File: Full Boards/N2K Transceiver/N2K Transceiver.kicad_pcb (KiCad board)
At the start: 4 copper layers, 80 x 60 mm, 73 parts, among them J1 JTAG, SW1 SW_MEC_5G, SW2 SW_MEC_5G, SW3 SW_MEC_5G

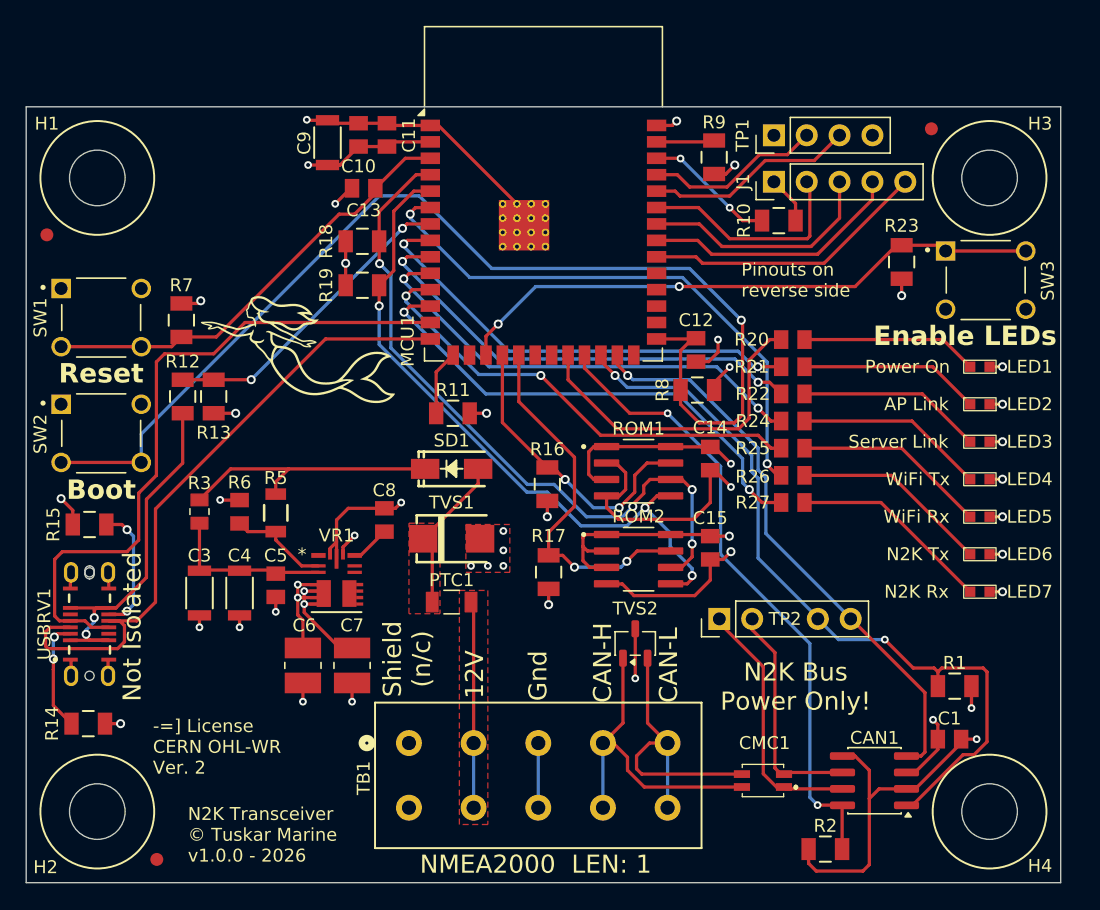
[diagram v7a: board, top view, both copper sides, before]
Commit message: Updated annotations after the RC removal.
Signed-off-by: digimer <digital.mermaid@gmail.com>
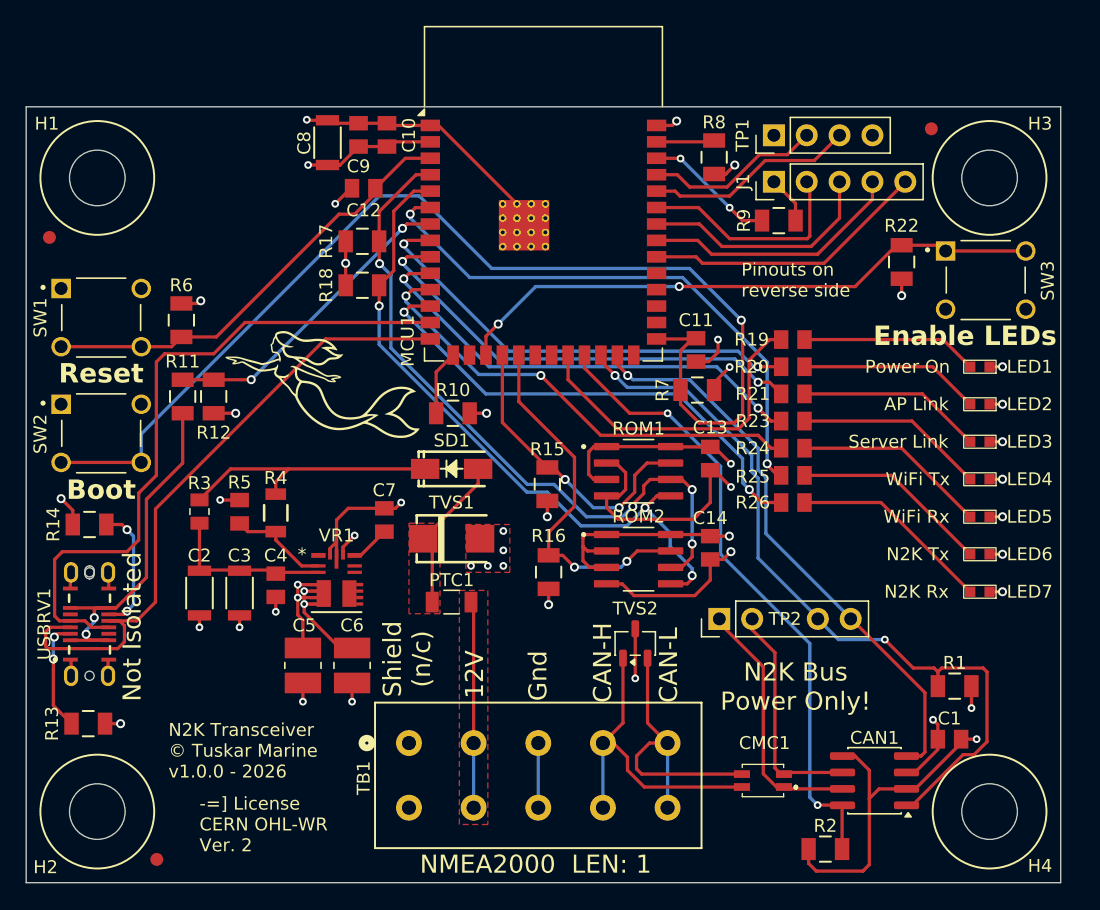
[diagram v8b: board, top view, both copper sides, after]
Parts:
- moved REF** 3.30 mm to (64.4, 53.3)
- moved FID2 0.28 mm to (61.8, 53.4)
- renumbered C11 to C10, C12 to C11, C13 to C12, C14 to C13, C15 to C14, C3 to C2, C4 to C3, C5 to C4, C6 to C5, C7 to C6, C8 to C7, C9 to C8, C10 to C9, R11 to R10, R12 to R11, R13 to R12, R14 to R13, R15 to R14, R16 to R15, R17 to R16, R18 to R17, R19 to R18, R20 to R19, R21 to R20, R22 to R21, R23 to R22, R24 to R23, R25 to R24, R26 to R25, R27 to R26, R5 to R4, R6 to R5, R7 to R6, R8 to R7, R9 to R8, R10 to R9
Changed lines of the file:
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@@
 		(layer "F.Cu")
 		(at 119.3 69.7)
-		(property "Reference" "R25"
+		(property "Reference" "R24"
 			(at -3.1162 0 0)
 			(unlocked yes)
@@
 		(at 100.3 72.480916 90)
 		(tags "RNCP1206FTD3K01 ")
-		(property "Reference" "R16"
+		(property "Reference" "R15"
 			(at 2.7 0 0)
 			(unlocked yes)
@@
 		(at 127.7 55.3 -90)
 		(tags "RNCP1206FTD3K01 ")
-		(property "Reference" "R23"
+		(property "Reference" "R22"
 			(at -2.8 0 0)
 			(unlocked yes)
@@
 		(layer "F.Cu")
 		(at 79.3 74.7 90)
-		(property "Reference" "R5"
+		(property "Reference" "R4"
 			(at 2.7 0 180)
 			(layer "F.SilkS")
@@
 		(at 112.9 70.5 90)
 		(tags "08051C105K4Z2A ")
-		(property "Reference" "C14"
+		(property "Reference" "C13"
 			(at 2.4 0 0)
 			(unlocked yes)
@@
 		(at 87.7 75.25 90)
 		(tags "08051C105K4Z2A ")
-		(property "Reference" "C8"
+		(property "Reference" "C7"
 			(at 2.3 0 0)
 			(unlocked yes)
@@
 		(at 111.8 62.1 -90)
 		(tags "08051C105K4Z2A ")
-		(property "Reference" "C12"
+		(property "Reference" "C11"
 			(at -2.3 0 0)
 			(unlocked yes)
@@
 		(layer "F.Cu")
 		(at 119.3 71.8)
-		(property "Reference" "R26"
+		(property "Reference" "R25"
 			(at -3.1162 0.1 0)
 			(unlocked yes)
@@
 	(footprint "Fiducial:Fiducial_1mm_Mask2mm"
 		(layer "F.Cu")
-		(at 61.6 53.2)
+		(at 61.8 53.4)
 		(descr "Fiducial, circular marking, 1mm bare copper, 2mm soldermask opening (Level A)")
 		(tags "fiducial")
@@
 		(at 64.8 91)
 		(tags "RNCP1206FTD3K01 ")
-		(property "Reference" "R14"
+		(property "Reference" "R13"
 			(at -2.8 0 90)
 			(unlocked yes)
@@
 		(at 85.7 45.472 90)
 		(tags "08051C105K4Z2A ")
-		(property "Reference" "C10"
+		(property "Reference" "C9"
 			(at -2.428 0 0)
 			(unlocked yes)
@@
 		(layer "F.Cu")
 		(at 119.3 63.4)
-		(property "Reference" "R21"
+		(property "Reference" "R20"
 			(at -3.2 0 0)
 			(unlocked yes)
@@
 		(at 118.2 52.1 180)
 		(tags "RNCP1206FTD3K01 ")
-		(property "Reference" "R10"
+		(property "Reference" "R9"
 			(at 2.7 0 90)
 			(unlocked yes)
@@
 		(at 86.1 49.6 180)
 		(tags "08051C105K4Z2A ")
-		(property "Reference" "C13"
+		(property "Reference" "C12"
 			(at 0 -1.7 0)
 			(unlocked yes)
@@
 		(at 113.2 47.2 90)
 		(tags "RNCP1206FTD3K01 ")
-		(property "Reference" "R9"
+		(property "Reference" "R8"
 			(at 2.7 0 0)
 			(unlocked yes)
@@
 		(at 112.9 77.4 90)
 		(tags "08051C105K4Z2A ")
-		(property "Reference" "C15"
+		(property "Reference" "C14"
 			(at 2.3 0 0)
 			(unlocked yes)
@@
 		(layer "F.Cu")
 		(at 119.3 65.5)
-		(property "Reference" "R22"
+		(property "Reference" "R21"
 			(at -3.1162 0 0)
 			(unlocked yes)
@@
 		(at 73.4 80.9 -90)
 		(tags "CGA5L1X7R1H106K160AE ")
-		(property "Reference" "C3"
+		(property "Reference" "C2"
 			(at -2.9 0 0)
 			(unlocked yes)
@@
 		(at 83.3 46.072 -90)
 		(tags "CGA5L1X7R1H106K160AE ")
-		(property "Reference" "C9"
+		(property "Reference" "C8"
 			(at 0.028 1.8 90)
 			(unlocked yes)
@@
 		(at 111.9 65.2)
 		(tags "RNCP1206FTD3K01 ")
-		(property "Reference" "R8"
+		(property "Reference" "R7"
 			(at -2.7 0 90)
 			(unlocked yes)
@@
 		(at 93 67 180)
 		(tags "RNCP1206FTD3K01 ")
-		(property "Reference" "R11"
+		(property "Reference" "R10"
 			(at 0 1.8 0)
 			(unlocked yes)
@@
 	(footprint "mr-stuff:Mermaid Silkscreen - 10mm"
 		(layer "F.Cu")
-		(at 62.52748 50.638629)
+		(at 64.42748 53.338629)
 		(property "Reference" "REF**"
 			(at 0 -0.5 0)
@@
 		(at 76.5 80.9 -90)
 		(tags "CGA5L1X7R1H106K160AE ")
-		(property "Reference" "C4"
+		(property "Reference" "C3"
 			(at -2.9 0 0)
 			(unlocked yes)
@@
 		(at 86 53.7 180)
 		(tags "RNCP1206FTD3K01 ")
-		(property "Reference" "R18"
+		(property "Reference" "R17"
 			(at 2.8 0 90)
 			(unlocked yes)
@@
 		(layer "F.Cu")
 		(at 119.3 67.6)
-		(property "Reference" "R24"
+		(property "Reference" "R23"
 			(at -3.1 0 0)
 			(unlocked yes)
@@
 		(layer "F.Cu")
 		(at 76.5 74.6 90)
-		(property "Reference" "R6"
+		(property "Reference" "R5"
 			(at 2.2537 0 0)
 			(unlocked yes)
@@
 		(at 72.1 65.7 90)
 		(tags "RNCP1206FTD3K01 ")
-		(property "Reference" "R12"
+		(property "Reference" "R11"
 			(at 2.7 0 0)
 			(unlocked yes)
@@
 		(layer "F.Cu")
 		(at 119.3 73.9)
-		(property "Reference" "R27"
+		(property "Reference" "R26"
 			(at -3.1162 0 0)
 			(unlocked yes)
@@
 		(layer "F.Cu")
 		(at 85.2 86.5 -90)
-		(property "Reference" "C7"
+		(property "Reference" "C6"
 			(at -3.1 0 0)
 			(layer "F.SilkS")
@@
 		(layer "F.Cu")
 		(at 81.4 86.5 -90)
-		(property "Reference" "C6"
+		(property "Reference" "C5"
 			(at -3.1 -0.1 0)
 			(layer "F.SilkS")
@@
 		(at 86 57.1 180)
 		(tags "RNCP1206FTD3K01 ")
-		(property "Reference" "R19"
+		(property "Reference" "R18"
 			(at 2.8 0 90)
 			(unlocked yes)
@@
 		(at 100.4 79.280916 90)
 		(tags "RNCP1206FTD3K01 ")
-		(property "Reference" "R17"
+		(property "Reference" "R16"
 			(at 2.8 0 0)
 			(unlocked yes)
@@
 		(at 79.3 80.3 -90)
 		(tags "08051C105K4Z2A ")
-		(property "Reference" "C5"
+		(property "Reference" "C4"
 			(at -2.3 0 0)
 			(unlocked yes)
@@
 		(at 72 59.8 90)
 		(tags "RNCP1206FTD3K01 ")
-		(property "Reference" "R7"
+		(property "Reference" "R6"
 			(at 2.7 0 0)
 			(unlocked yes)
@@
 		(at 64.9 75.6 180)
 		(tags "RNCP1206FTD3K01 ")
-		(property "Reference" "R15"
+		(property "Reference" "R14"
 			(at 2.8 0 90)
 			(unlocked yes)
@@
 		(layer "F.Cu")
 		(at 119.3 61.3)
-		(property "Reference" "R20"
+		(property "Reference" "R19"
 			(at -3.2 0 0)
 			(unlocked yes)
@@
 		(at 74.5 65.7 90)
 		(tags "RNCP1206FTD3K01 ")
-		(property "Reference" "R13"
+		(property "Reference" "R12"
 			(at -2.8 0 0)
 			(unlocked yes)
@@
 		(at 87.9 45.472 90)
 		(tags "08051C105K4Z2A ")
-		(property "Reference" "C11"
+		(property "Reference" "C10"
 			(at -0.028 1.7 90)
 			(unlocked yes)
@@
 		(layer "Edge.Cuts")
 	)
-	(gr_text "-=] License\nCERN OHL-WR\nVer. 2\n"
-		(at 69.8 90.6 0)
+	(gr_text "N2K Transceiver\n© Tuskar Marine\nv1.0.0 - 2026"
+		(at 71 90.9 0)
 		(layer "F.SilkS")
 		(effects
@@
 		)
 	)
-	(gr_text "N2K Transceiver\n© Tuskar Marine\nv1.0.0 - 2026"
-		(at 72.5 97.4 0)
+	(gr_text "-=] License\nCERN OHL-WR\nVer. 2\n"
+		(at 73.4 96.6 0)
 		(layer "F.SilkS")
 		(effects
